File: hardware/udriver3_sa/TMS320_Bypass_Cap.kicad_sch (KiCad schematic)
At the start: 44 parts

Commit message: Second release of uOmodri Single Axis (uOmodri_SA).
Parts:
- added C88: 100n, Capacitor_SMD:C_0201_0603Metric, symbol Device:C
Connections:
- net GNDA: now also C88.2
- net REF_3V0_BUF: now also C88.1
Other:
- moved on the sheet: C41, C42, C43

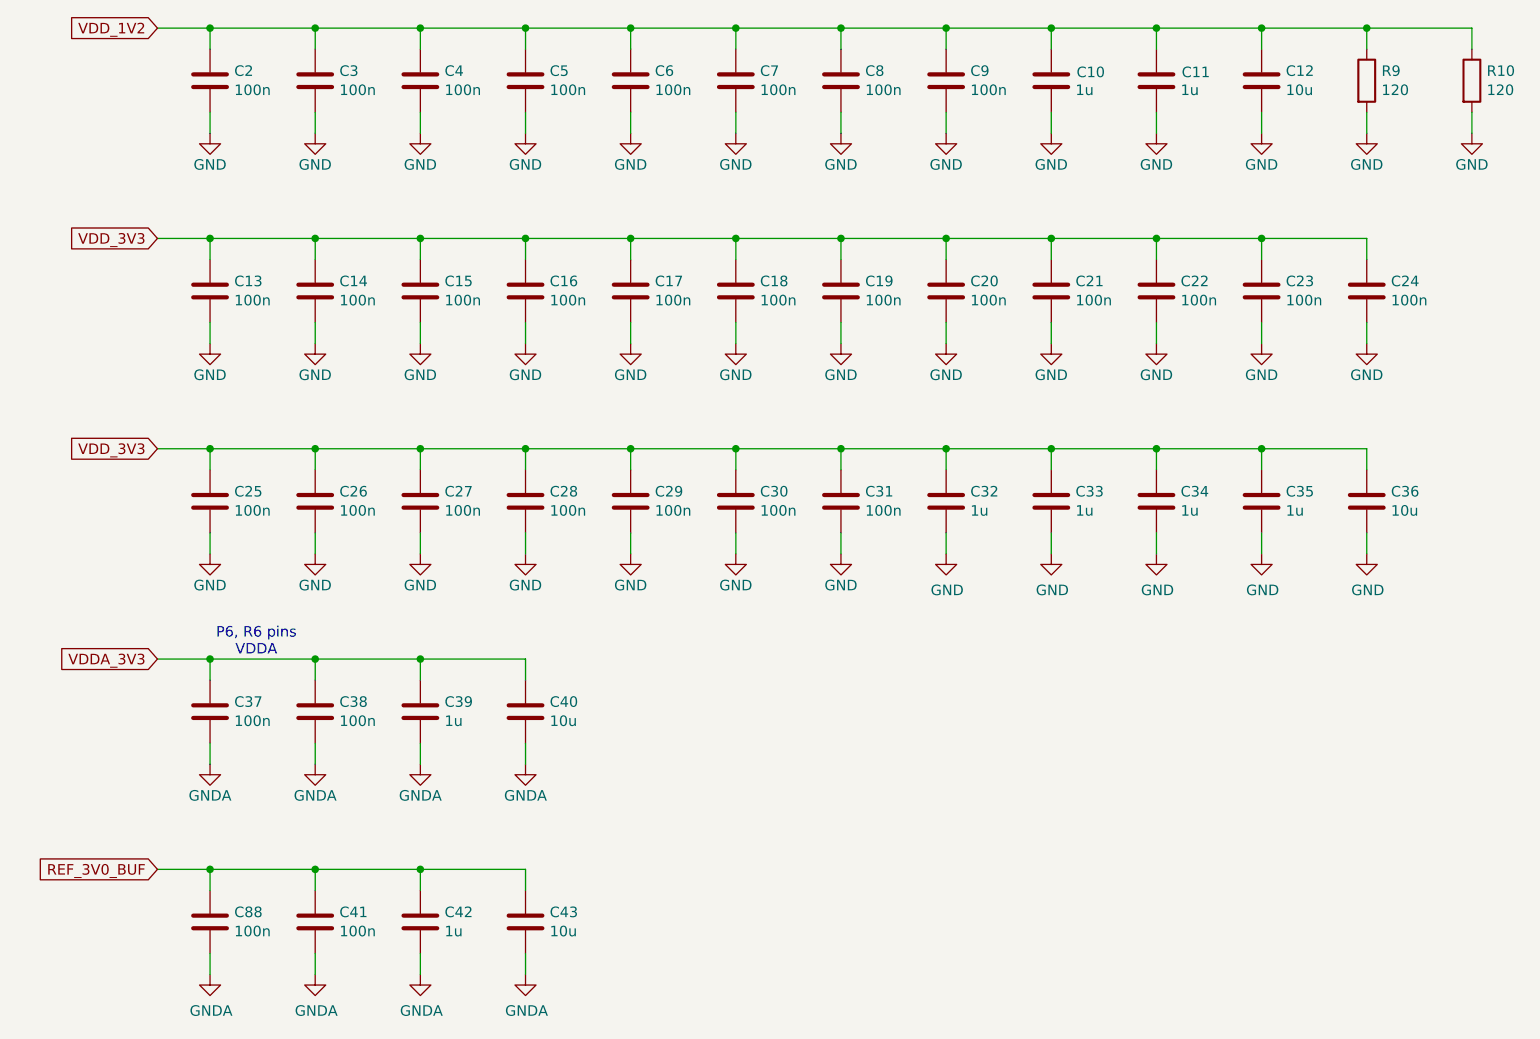
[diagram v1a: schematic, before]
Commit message: Update on uOmodri_SA. Remove USB, com SPI & debug connectors for integration into Myactuator motors. Connectors replaced by a ZIF connector.
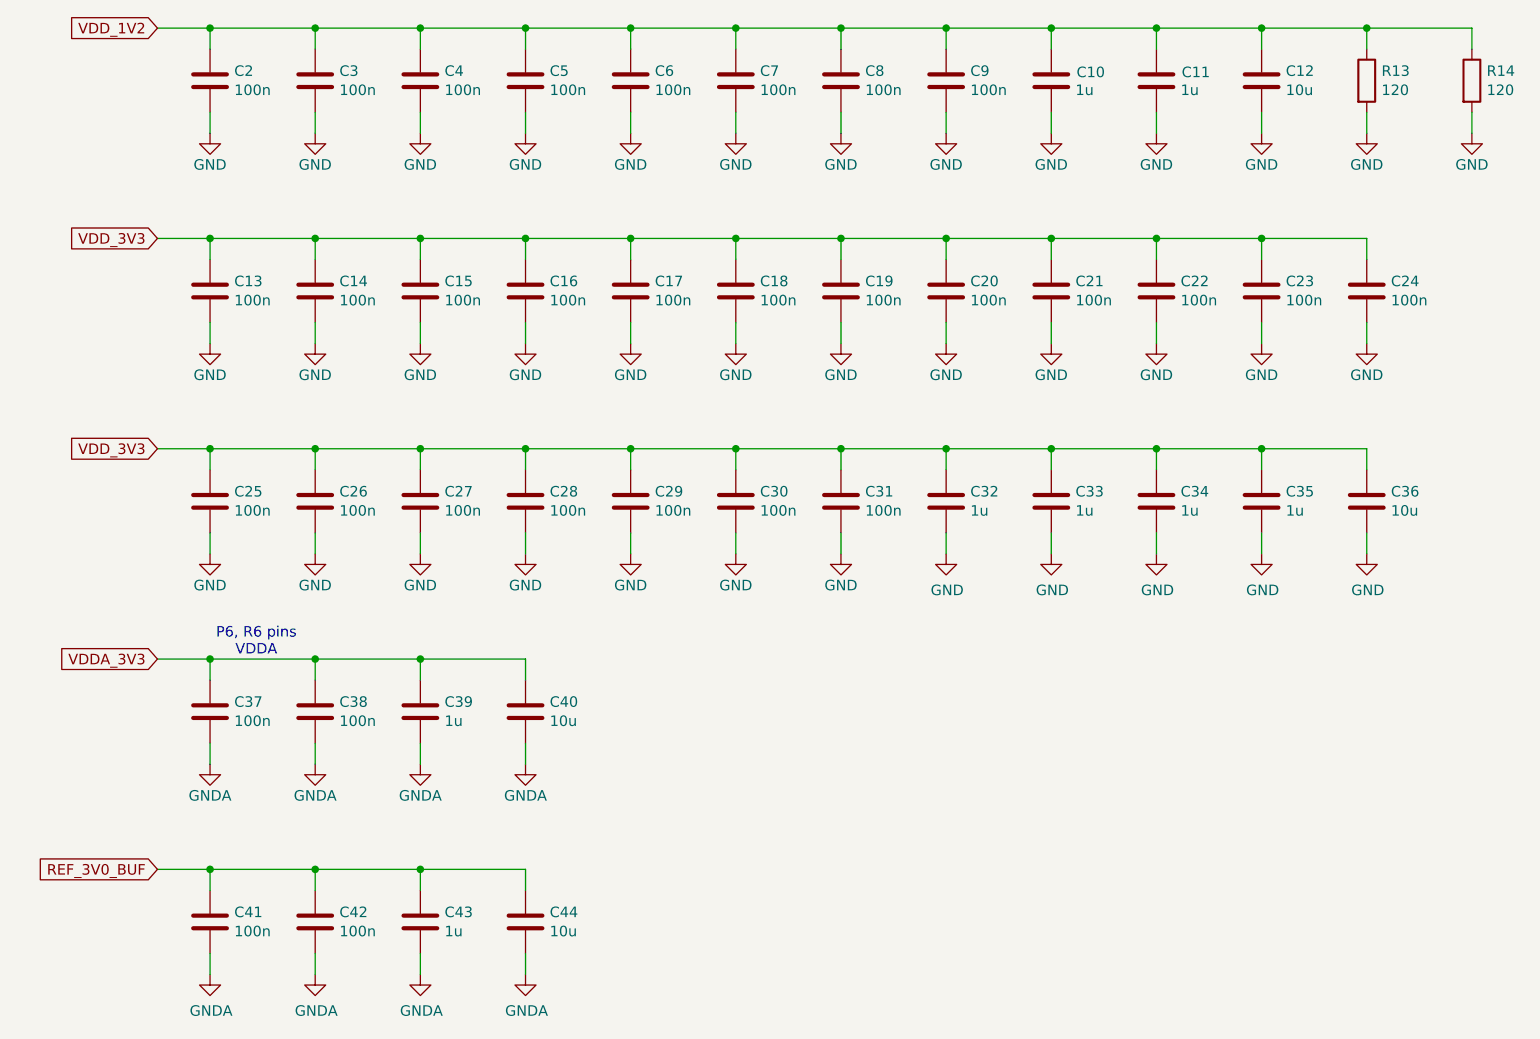
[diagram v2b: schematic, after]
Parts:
- renumbered C88 to C41, C41 to C42, C42 to C43, C43 to C44, R9 to R13, R10 to R14
